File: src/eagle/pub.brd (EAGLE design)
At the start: 63.5 x 63.5 mm, 27 parts, among them IC1 PIC18F25K50, SW1 EC12E_SW

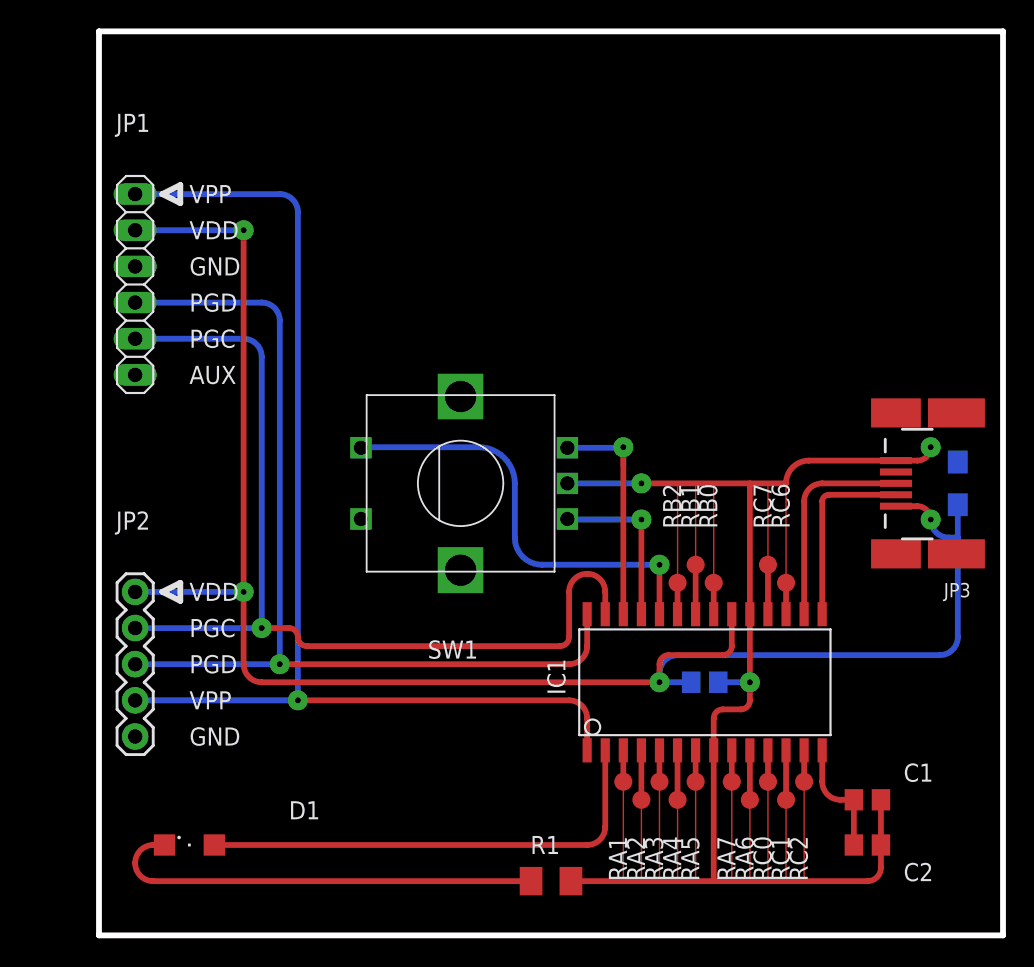
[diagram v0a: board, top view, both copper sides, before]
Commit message: Tweaked PCB slightly
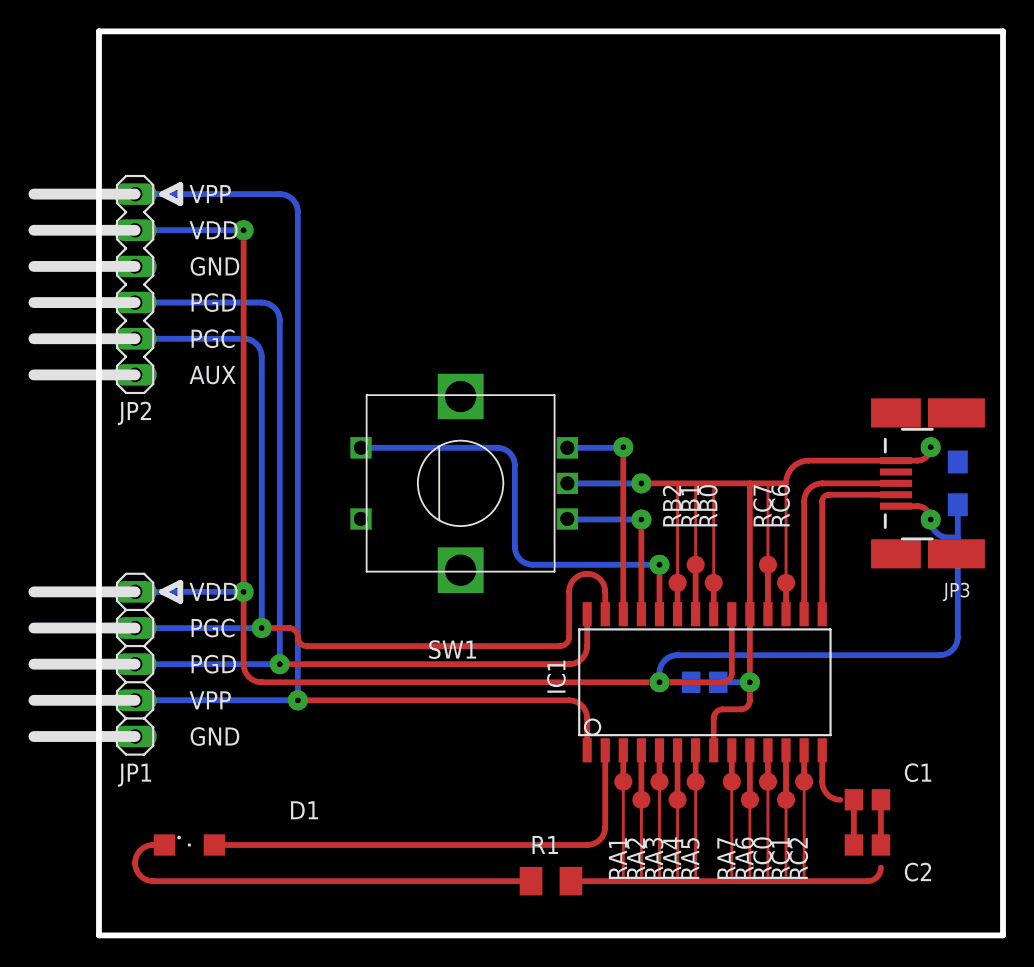
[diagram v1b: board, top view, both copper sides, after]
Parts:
- JP1: value PICKIT -> MIKROPROG; device pinhead:1X06 -> pub:1X05/90
- JP2: value MIKROPROG -> PICKKIT; device SparkFun-Connectors:1X05 -> pub:1X06/90
- moved JP1 26.7 mm to (2.54, 19.1), turned to 90 degrees
- moved JP2 21.6 mm to (2.54, 45.7), turned to 90 degrees
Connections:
- net GND: now also JP1.5, JP2.3, JP3.MNT1, JP3.MNT2, JP3.MNT3, JP3.MNT4; no longer JP1.3, JP2.5
- net N$10: now also JP1.4, JP2.1; no longer JP1.1, JP2.4
- net N$7: now also JP1.1, JP2.2; no longer JP1.2, JP2.1
- net N$8: now also JP1.2, JP2.5; no longer JP1.5, JP2.2
- net N$9: now also JP1.3, JP2.4; no longer JP1.4, JP2.3
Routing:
- net GND: track 263.7 -> 252.9 mm
- net N$1: track 16.9 -> 15.7 mm
- net RA1: track 30.1 -> 31.2 mm
- net N$3: track 8.13 -> 7.18 mm
